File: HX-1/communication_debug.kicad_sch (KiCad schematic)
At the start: 21 parts, among them J1 USB_C_Receptacle_USB2.0_16P, U2 USBLC6-2SC6, U4 LSM6DS3

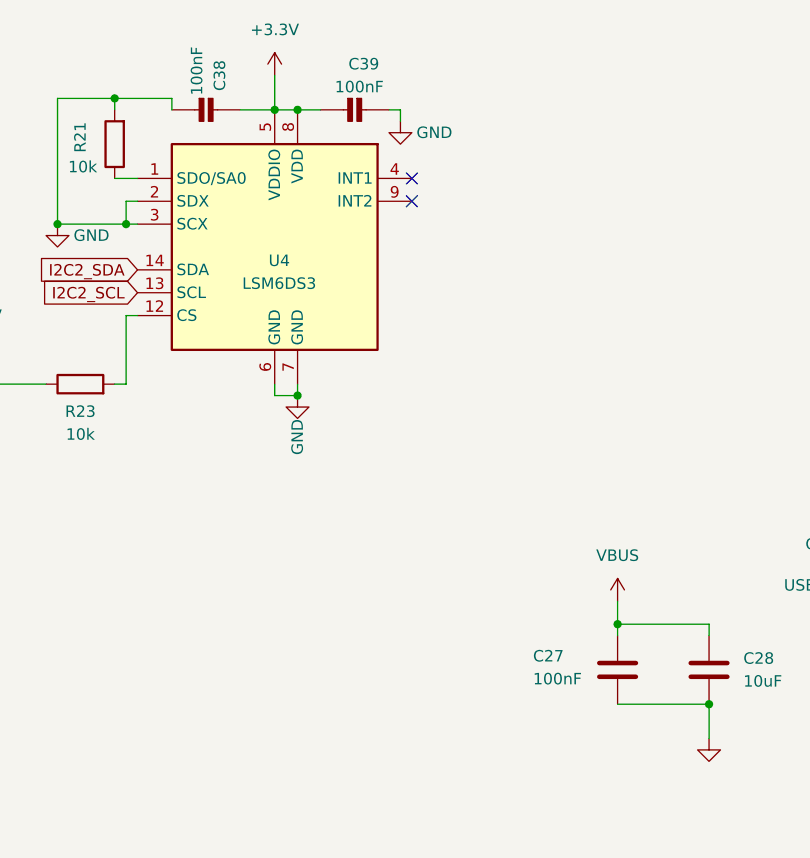
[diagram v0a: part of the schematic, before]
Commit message: change most passive components to 0402 to save space
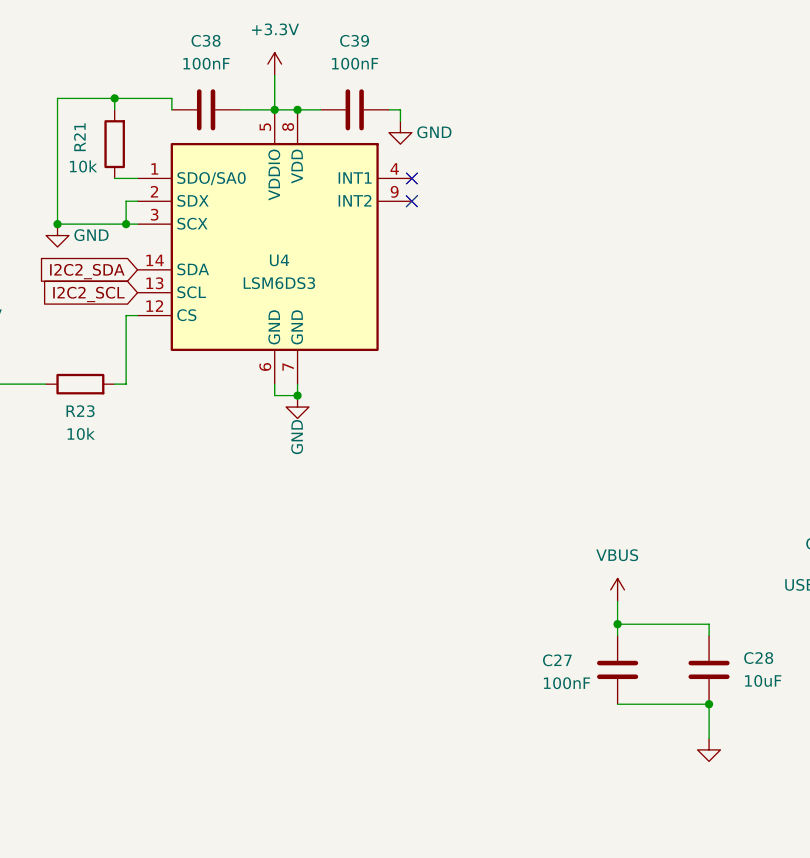
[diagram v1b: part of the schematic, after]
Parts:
- removed C38, C39: 100nF, Capacitor_SMD:C_0603_1608Metric, symbol MPL3115A2_v0.2-eagle-import:CAP_CERAMIC0805-NOOUTLINE
- added C38, C39: 100nF, Capacitor_SMD:C_0402_1005Metric, symbol Device:C
- C27: footprint Capacitor_SMD:C_0603_1608Metric -> Capacitor_SMD:C_0402_1005Metric; LCSC PN C14663 -> C1525
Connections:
- net +3.3V: now also C38.2, C39.1
- net GND: now also C27.2, C38.1, C39.2; no longer C27.1
- net VBUS: now also C27.1; no longer C27.2
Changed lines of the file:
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@@
-	)
-	(symbol
-		(lib_id "MPL3115A2_v0.2-eagle-import:CAP_CERAMIC0805-NOOUTLINE")
-		(at 46.99 31.75 270)
-		(unit 1)
-		(exclude_from_sim no)
-		(in_bom yes)
-		(on_board yes)
-		(dnp no)
-		(property "Reference" "C38"
-			(at 49.784 27.94 0)
-			(effects
-				(font
-					(size 1.27 1.27)
-				)
-			)
-		)
-		(property "Value" "100nF"
-			(at 47.244 27.432 0)
-			(effects
-				(font
-					(size 1.27 1.27)
-				)
-			)
-		)
-		(property "Footprint" "Capacitor_SMD:C_0603_1608Metric"
-			(at 46.99 31.75 0)
-			(effects
-				(font
-					(size 1.27 1.27)
-				)
-				(hide yes)
-			)
-		)
-		(property "Datasheet" ""
-			(at 46.99 31.75 0)
-			(effects
-				(font
-					(size 1.27 1.27)
-				)
-				(hide yes)
-			)
-		)
-		(property "Description" ""
-			(at 46.99 31.75 0)
-			(effects
-				(font
-					(size 1.27 1.27)
-				)
-				(hide yes)
-			)
-		)
-		(property "LCSC" "C14663"
-			(at 46.99 31.75 0)
-			(effects
-				(font
-					(size 1.27 1.27)
-				)
-				(hide yes)
-			)
-		)
-		(pin "1"
-		)
-		(pin "2"
-		)
-		(instances
-			(project "HX-1"
-				(path "/a3219989-2bf1-44ea-9412-fab86edfb39b/f68304e7-586c-4481-9c91-394c7e636be5"
-					(reference "C38")
-					(unit 1)
-				)
-			)
-		)
 	)
 	(symbol
@@
 	)
 	(symbol
-		(lib_id "MPL3115A2_v0.2-eagle-import:CAP_CERAMIC0805-NOOUTLINE")
-		(at 63.5 31.75 270)
-		(unit 1)
-		(exclude_from_sim no)
-		(in_bom yes)
-		(on_board yes)
-		(dnp no)
-		(property "Reference" "C39"
-			(at 65.786 26.67 90)
-			(effects
-				(font
-					(size 1.27 1.27)
-				)
-			)
-		)
-		(property "Value" "100nF"
-			(at 65.278 29.21 90)
-			(effects
-				(font
-					(size 1.27 1.27)
-				)
-			)
-		)
-		(property "Footprint" "Capacitor_SMD:C_0603_1608Metric"
-			(at 63.5 31.75 0)
-			(effects
-				(font
-					(size 1.27 1.27)
-				)
-				(hide yes)
-			)
-		)
-		(property "Datasheet" ""
-			(at 63.5 31.75 0)
-			(effects
-				(font
-					(size 1.27 1.27)
-				)
-				(hide yes)
-			)
-		)
-		(property "Description" ""
-			(at 63.5 31.75 0)
-			(effects
-				(font
-					(size 1.27 1.27)
-				)
-				(hide yes)
-			)
-		)
-		(property "LCSC" "C14663"
-			(at 63.5 31.75 0)
-			(effects
-				(font
-					(size 1.27 1.27)
-				)
-				(hide yes)
-			)
-		)
-		(pin "1"
-		)
-		(pin "2"
-		)
-		(instances
-			(project "HX-1"
-				(path "/a3219989-2bf1-44ea-9412-fab86edfb39b/f68304e7-586c-4481-9c91-394c7e636be5"
-					(reference "C39")
-					(unit 1)
-				)
-			)
-		)
-	)
-	(symbol
 		(lib_id "power:GND")
 		(at 175.26 114.3 0)
@@
 	)
 	(symbol
+		(lib_id "Device:C")
+		(at 64.77 31.75 90)
+		(unit 1)
+		(exclude_from_sim no)
+		(in_bom yes)
+		(on_board yes)
+		(dnp no)
+		(fields_autoplaced yes)
+		(property "Reference" "C39"
+			(at 64.77 24.13 90)
+			(effects
+				(font
+					(size 1.27 1.27)
+				)
+			)
+		)
+		(property "Value" "100nF"
+			(at 64.77 26.67 90)
+			(effects
+				(font
+					(size 1.27 1.27)
+				)
+			)
+		)
+		(property "Footprint" "Capacitor_SMD:C_0402_1005Metric"
+			(at 68.58 30.7848 0)
+			(effects
+				(font
+					(size 1.27 1.27)
+				)
+				(hide yes)
+			)
+		)
+		(property "Datasheet" "~"
+			(at 64.77 31.75 0)
+			(effects
+				(font
+					(size 1.27 1.27)
+				)
+				(hide yes)
+			)
+		)
+		(property "Description" "Unpolarized capacitor"
+			(at 64.77 31.75 0)
+			(effects
+				(font
+					(size 1.27 1.27)
+				)
+				(hide yes)
+			)
+		)
+		(property "LCSC PN" "C1525"
+			(at 64.77 31.75 0)
+			(effects
+				(font
+					(size 1.27 1.27)
+				)
+				(hide yes)
+			)
+		)
+		(pin "2"
+		)
+		(pin "1"
+		)
+		(instances
+			(project "HX-1"
+				(path "/a3219989-2bf1-44ea-9412-fab86edfb39b/f68304e7-586c-4481-9c91-394c7e636be5"
+					(reference "C39")
+					(unit 1)
+				)
+			)
+		)
+	)
+	(symbol
 		(lib_id "power:GND")
 		(at 118.11 144.78 0)
@@
 	)
 	(symbol
+		(lib_id "Device:C")
+		(at 48.26 31.75 90)
+		(unit 1)
+		(exclude_from_sim no)
+		(in_bom yes)
+		(on_board yes)
+		(dnp no)
+		(fields_autoplaced yes)
+		(property "Reference" "C38"
+			(at 48.26 24.13 90)
+			(effects
+				(font
+					(size 1.27 1.27)
+				)
+			)
+		)
+		(property "Value" "100nF"
+			(at 48.26 26.67 90)
+			(effects
+				(font
+					(size 1.27 1.27)
+				)
+			)
+		)
+		(property "Footprint" "Capacitor_SMD:C_0402_1005Metric"
+			(at 52.07 30.7848 0)
+			(effects
+				(font
+					(size 1.27 1.27)
+				)
+				(hide yes)
+			)
+		)
+		(property "Datasheet" "~"
+			(at 48.26 31.75 0)
+			(effects
+				(font
+					(size 1.27 1.27)
+				)
+				(hide yes)
+			)
+		)
+		(property "Description" "Unpolarized capacitor"
+			(at 48.26 31.75 0)
+			(effects
+				(font
+					(size 1.27 1.27)
+				)
+				(hide yes)
+			)
+		)
+		(property "LCSC PN" "C1525"
+			(at 48.26 31.75 0)
+			(effects
+				(font
+					(size 1.27 1.27)
+				)
+				(hide yes)
+			)
+		)
+		(pin "2"
+		)
+		(pin "1"
+		)
+		(instances
+			(project "HX-1"
+				(path "/a3219989-2bf1-44ea-9412-fab86edfb39b/f68304e7-586c-4481-9c91-394c7e636be5"
+					(reference "C38")
+					(unit 1)
+				)
+			)
+		)
+	)
+	(symbol
 		(lib_id "power:GND")
 		(at 58.42 63.5 0)
@@
 	)
 	(symbol
-		(lib_id "Device:C")
-		(at 93.98 93.98 180)
-		(unit 1)
-		(exclude_from_sim no)
-		(in_bom yes)
-		(on_board yes)
-		(dnp no)
-		(property "Reference" "C27"
-			(at 84.582 92.456 0)
-			(effects
-				(font
-					(size 1.27 1.27)
-				)
-				(justify right)
-			)
-		)
-		(property "Value" "100nF"
-			(at 84.582 94.996 0)
-			(effects
-				(font
-					(size 1.27 1.27)
-				)
-				(justify right)
-			)
-		)
-		(property "Footprint" "Capacitor_SMD:C_0603_1608Metric"
-			(at 93.0148 90.17 0)
-			(effects
-				(font
-					(size 1.27 1.27)
-				)
-				(hide yes)
-			)
-		)
-		(property "Datasheet" "~"
-			(at 93.98 93.98 0)
-			(effects
-				(font
-					(size 1.27 1.27)
-				)
-				(hide yes)
-			)
-		)
-		(property "Description" "Unpolarized capacitor"
-			(at 93.98 93.98 0)
-			(effects
-				(font
-					(size 1.27 1.27)
-				)
-				(hide yes)
-			)
-		)
-		(property "LCSC PN" "C14663"
-			(at 93.98 93.98 0)
-			(effects
-				(font
-					(size 1.27 1.27)
-				)
-				(hide yes)
-			)
-		)
-		(pin "2"
-		)
-		(pin "1"
-		)
-		(instances
-			(project "HX-1"
-				(path "/a3219989-2bf1-44ea-9412-fab86edfb39b/f68304e7-586c-4481-9c91-394c7e636be5"
-					(reference "C27")
-					(unit 1)
-				)
-			)
-		)
-	)
-	(symbol
 		(lib_id "Device:D_Schottky")
 		(at 149.86 67.31 270)
@@
 					(unit 1)
 				)
+			)
+		)
+	)
+	(symbol
+		(lib_id "Device:C")
+		(at 93.98 93.98 0)
+		(unit 1)
+		(exclude_from_sim no)
+		(in_bom yes)
+		(on_board yes)
+		(dnp no)
+		(property "Reference" "C27"
+			(at 85.598 92.964 0)
+			(effects
+				(font
+					(size 1.27 1.27)
+				)
+				(justify left)
+			)
+		)
+		(property "Value" "100nF"
+			(at 85.598 95.504 0)
+			(effects
+				(font
+					(size 1.27 1.27)
+				)
+				(justify left)
+			)
+		)
+		(property "Footprint" "Capacitor_SMD:C_0402_1005Metric"
+			(at 94.9452 97.79 0)
+			(effects
+				(font
+					(size 1.27 1.27)
+				)
+				(hide yes)
+			)
+		)
+		(property "Datasheet" "~"
+			(at 93.98 93.98 0)
+			(effects
+				(font
+					(size 1.27 1.27)
+				)
+				(hide yes)
+			)
+		)
+		(property "Description" "Unpolarized capacitor"
+			(at 93.98 93.98 0)
+			(effects
+				(font
+					(size 1.27 1.27)
+				)
+				(hide yes)
+			)
+		)
+		(property "LCSC PN" "C1525"
+			(at 93.98 93.98 0)
+			(effects
+				(font
+					(size 1.27 1.27)
+				)
+				(hide yes)
+			)
+		)
+		(pin "2"
+		)
+		(pin "1"
+		)
+		(instances
+			(project "HX-1"
+				(path "/a3219989-2bf1-44ea-9412-fab86edfb39b/f68304e7-586c-4481-9c91-394c7e636be5"
+					(reference "C27")
+					(unit 1)
+				)

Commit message: draft board size
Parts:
- added H1, H2, H3, H4: MountingHole_Pad, MountingHole:MountingHole_3.2mm_M3_Pad, symbol Mechanical:MountingHole_Pad
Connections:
- net GND: now also H1.1, H2.1, H3.1, H4.1
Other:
- note added: "Mounting Holes"

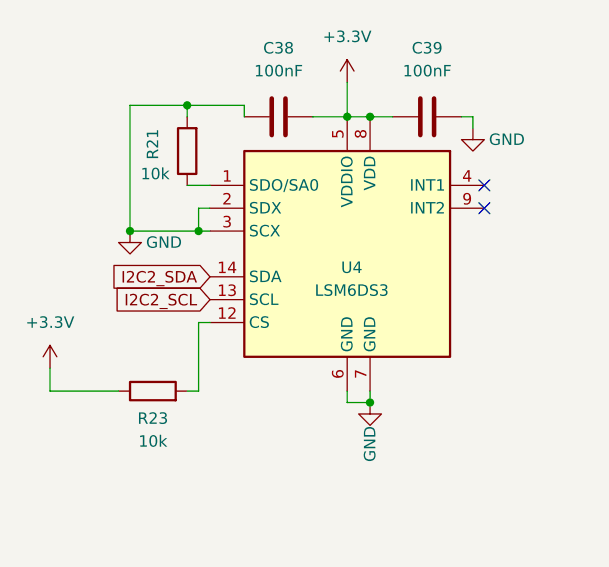
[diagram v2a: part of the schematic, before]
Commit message: change analog resistors to 0402 to make routing easier
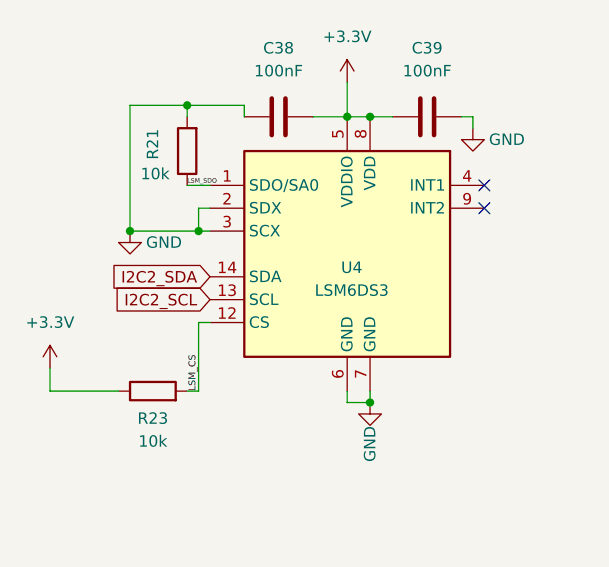
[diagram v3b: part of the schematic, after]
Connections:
- net LSM_CS: now reaches R23.2, U4.12 (CS)
- net LSM_SDO: now reaches R21.1, U4.1 (SDO/SA0)
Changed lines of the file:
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@@
+		)
+	)
+	(label "LSM_CS"
+		(at 39.37 62.23 90)
+		(effects
+			(font
+				(size 0.762 0.762)
+			)
+			(justify left bottom)
 		)
 	)
@@
 			)
 			(justify left bottom)
+		)
+	)
+	(label "LSM_SDO"
+		(at 38.1 39.37 0)
+		(effects
+			(font
+				(size 0.508 0.508)
+			)
+			(justify left bottom)

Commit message: change schottky diode to basic part from jlcpcb
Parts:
- D1, D2: footprint Diode_SMD:D_SOD-323F -> Diode_SMD:D_SOD-323; LCSC PN C146335 -> C191023
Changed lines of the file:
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@@
+	)
+	(symbol
+		(lib_id "Device:D_Schottky")
+		(at 167.64 67.31 270)
+		(unit 1)
+		(exclude_from_sim no)
+		(in_bom yes)
+		(on_board yes)
+		(dnp no)
+		(fields_autoplaced yes)
+		(property "Reference" "D2"
+			(at 170.18 65.7224 90)
+			(effects
+				(font
+					(size 1.27 1.27)
+				)
+				(justify left)
+			)
+		)
+		(property "Value" "D_Schottky"
+			(at 170.18 68.2624 90)
+			(effects
+				(font
+					(size 1.27 1.27)
+				)
+				(justify left)
+			)
+		)
+		(property "Footprint" "Diode_SMD:D_SOD-323"
+			(at 167.64 67.31 0)
+			(effects
+				(font
+					(size 1.27 1.27)
+				)
+				(hide yes)
+			)
+		)
+		(property "Datasheet" "~"
+			(at 167.64 67.31 0)
+			(effects
+				(font
+					(size 1.27 1.27)
+				)
+				(hide yes)
+			)
+		)
+		(property "Description" "Schottky diode"
+			(at 167.64 67.31 0)
+			(effects
+				(font
+					(size 1.27 1.27)
+				)
+				(hide yes)
+			)
+		)
+		(property "LCSC PN" "C191023"
+			(at 167.64 67.31 90)
+			(effects
+				(font
+					(size 1.27 1.27)
+				)
+				(hide yes)
+			)
+		)
+		(pin "1"
+		)
+		(pin "2"
+		)
+		(instances
+			(project "HX-1"
+				(path "/a3219989-2bf1-44ea-9412-fab86edfb39b/f68304e7-586c-4481-9c91-394c7e636be5"
+					(reference "D2")
+					(unit 1)
+				)
+			)
+		)
 	)
 	(symbol
@@
 	)
 	(symbol
-		(lib_id "Device:D_Schottky")
-		(at 167.64 67.31 270)
-		(unit 1)
-		(exclude_from_sim no)
-		(in_bom yes)
-		(on_board yes)
-		(dnp no)
-		(fields_autoplaced yes)
-		(property "Reference" "D2"
-			(at 170.18 65.7224 90)
-			(effects
-				(font
-					(size 1.27 1.27)
-				)
-				(justify left)
-			)
-		)
-		(property "Value" "D_Schottky"
-			(at 170.18 68.2624 90)
-			(effects
-				(font
-					(size 1.27 1.27)
-				)
-				(justify left)
-			)
-		)
-		(property "Footprint" "Diode_SMD:D_SOD-323F"
-			(at 167.64 67.31 0)
-			(effects
-				(font
-					(size 1.27 1.27)
-				)
-				(hide yes)
-			)
-		)
-		(property "Datasheet" "~"
-			(at 167.64 67.31 0)
-			(effects
-				(font
-					(size 1.27 1.27)
-				)
-				(hide yes)
-			)
-		)
-		(property "Description" "Schottky diode"
-			(at 167.64 67.31 0)
-			(effects
-				(font
-					(size 1.27 1.27)
-				)
-				(hide yes)
-			)
-		)
-		(property "LCSC PN" "C146335"
-			(at 167.64 67.31 90)
-			(effects
-				(font
-					(size 1.27 1.27)
-				)
-				(hide yes)
-			)
-		)
-		(pin "1"
-		)
-		(pin "2"
-		)
-		(instances
-			(project "HX-1"
-				(path "/a3219989-2bf1-44ea-9412-fab86edfb39b/f68304e7-586c-4481-9c91-394c7e636be5"
-					(reference "D2")
-					(unit 1)
-				)
-			)
-		)
-	)
-	(symbol
 		(lib_id "Jumper:SolderJumper_2_Bridged")
 		(at 149.86 53.34 90)
@@
 			)
 		)
-		(property "Footprint" "Diode_SMD:D_SOD-323F"
+		(property "Footprint" "Diode_SMD:D_SOD-323"
 			(at 149.86 67.31 0)
 			(effects
@@
 			)
 		)
-		(property "LCSC PN" "C146335"
+		(property "LCSC PN" "C191023"
 			(at 149.86 67.31 90)
 			(effects

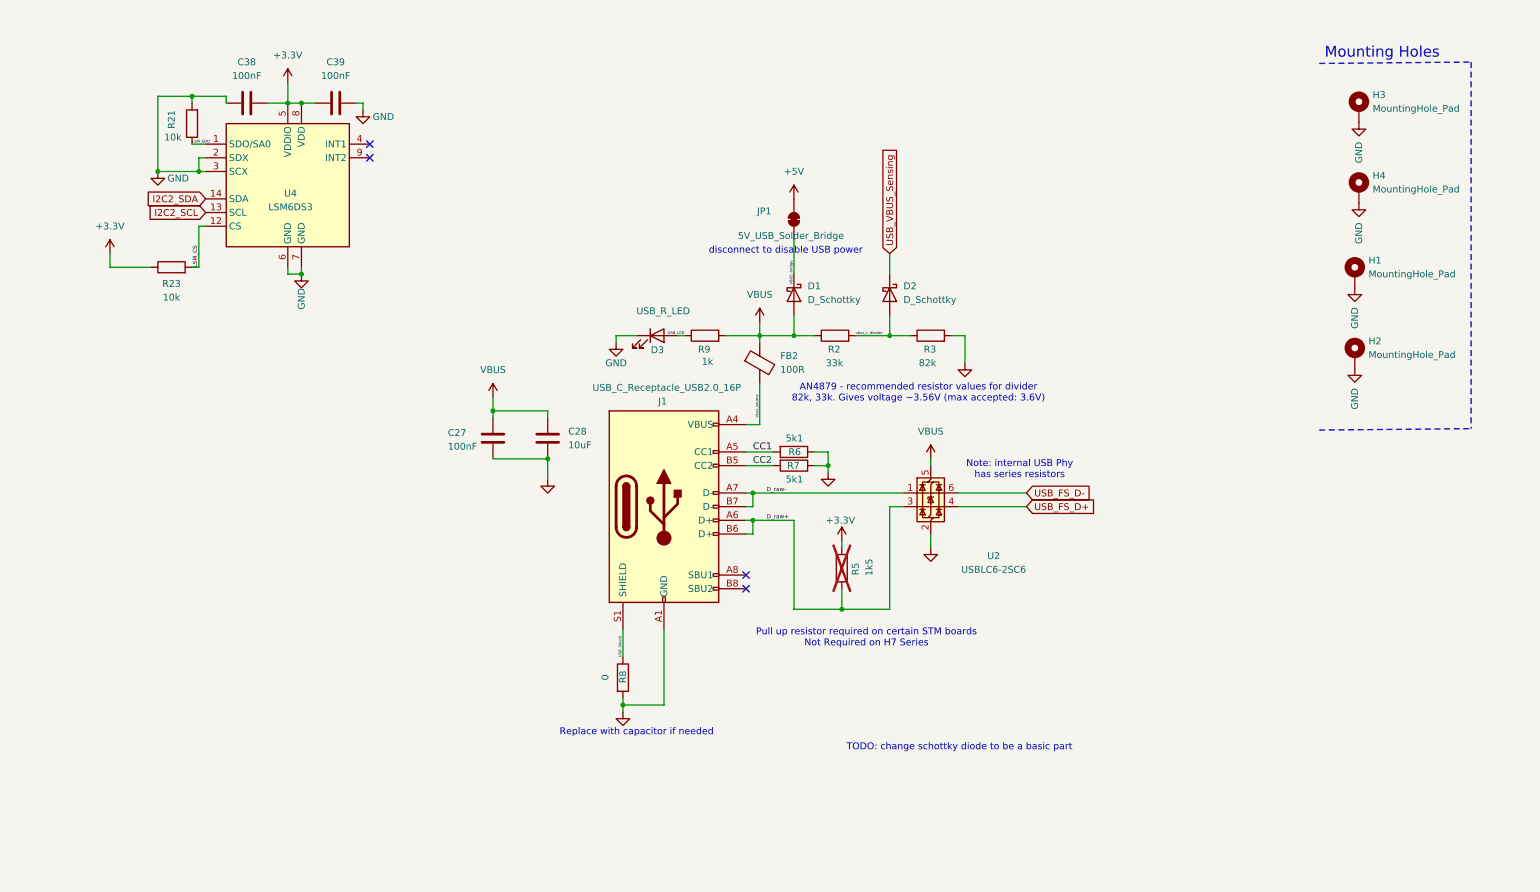
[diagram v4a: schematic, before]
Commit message: clean up schematic, layout more of pcb, fix some footprints
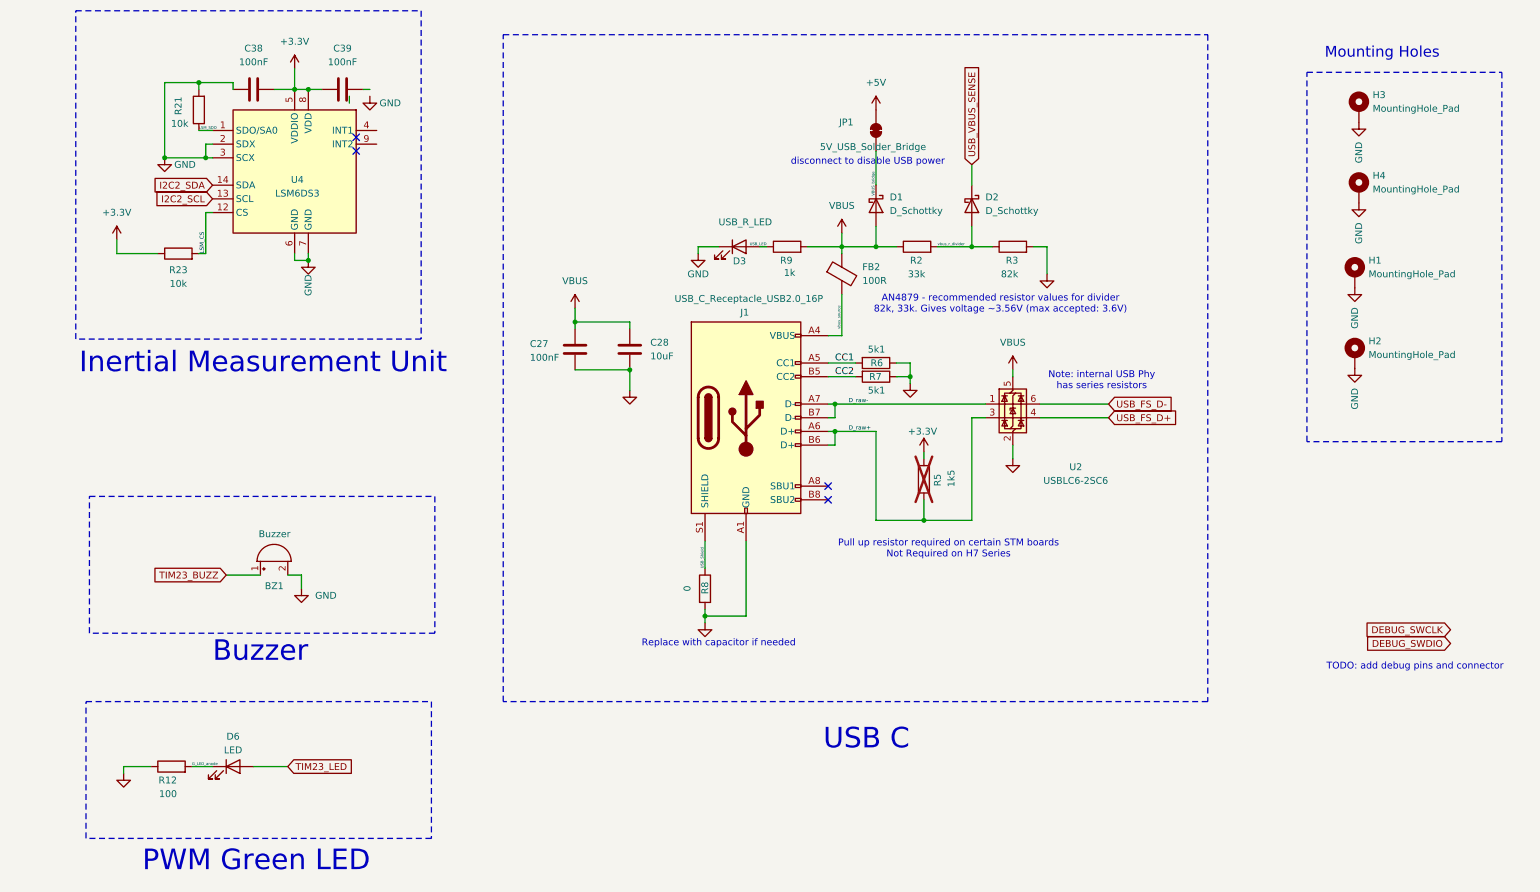
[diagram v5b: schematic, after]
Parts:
- added BZ1: Buzzer, Buzzer:YUEXIN YX-SMD5020, symbol Device:Buzzer
- added D6: LED, LED_SMD:LED_0805_2012Metric, symbol Device:LED
- added R12: 100, Resistor_SMD:R_0402_1005Metric, symbol Device:R
- R21, R23: footprint Resistor_SMD:R_0603_1608Metric -> Resistor_SMD:R_0402_1005Metric; LCSC PN (none) -> C25744
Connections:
- net GND: now also BZ1.2 (+), R12.1; no longer C39.2
- net USB_VBUS_Sensing renamed USB_VBUS_SENSE
- new net G_LED_anode: D6.1 (K), R12.2
- new net TIM23_BUZZ: BZ1.1 (-)
- new net TIM23_LED: D6.2 (A)
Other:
- note added: "Buzzer"
- note added: "Inertial Measurement Unit"
- note added: "PWM Green LED"
- note added: "TODO: add debug pins and connector"
- note added: "USB C"
- note removed: "TODO: change schottky diode to be a basic part"
- moved on the sheet: C27, C28, C38, C39, D1, D2, D3, FB2, J1, JP1, R2, R21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
